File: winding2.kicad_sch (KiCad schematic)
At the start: 13 parts, among them J1 Screw_Terminal_01x06, J2 Screw_Terminal_01x04, J3 Screw_Terminal_01x04, M1 Push_Button_W12mm, SW1 RotaryEncoder_Switch, U1 TMC2209_SILENTSTEPSTICK

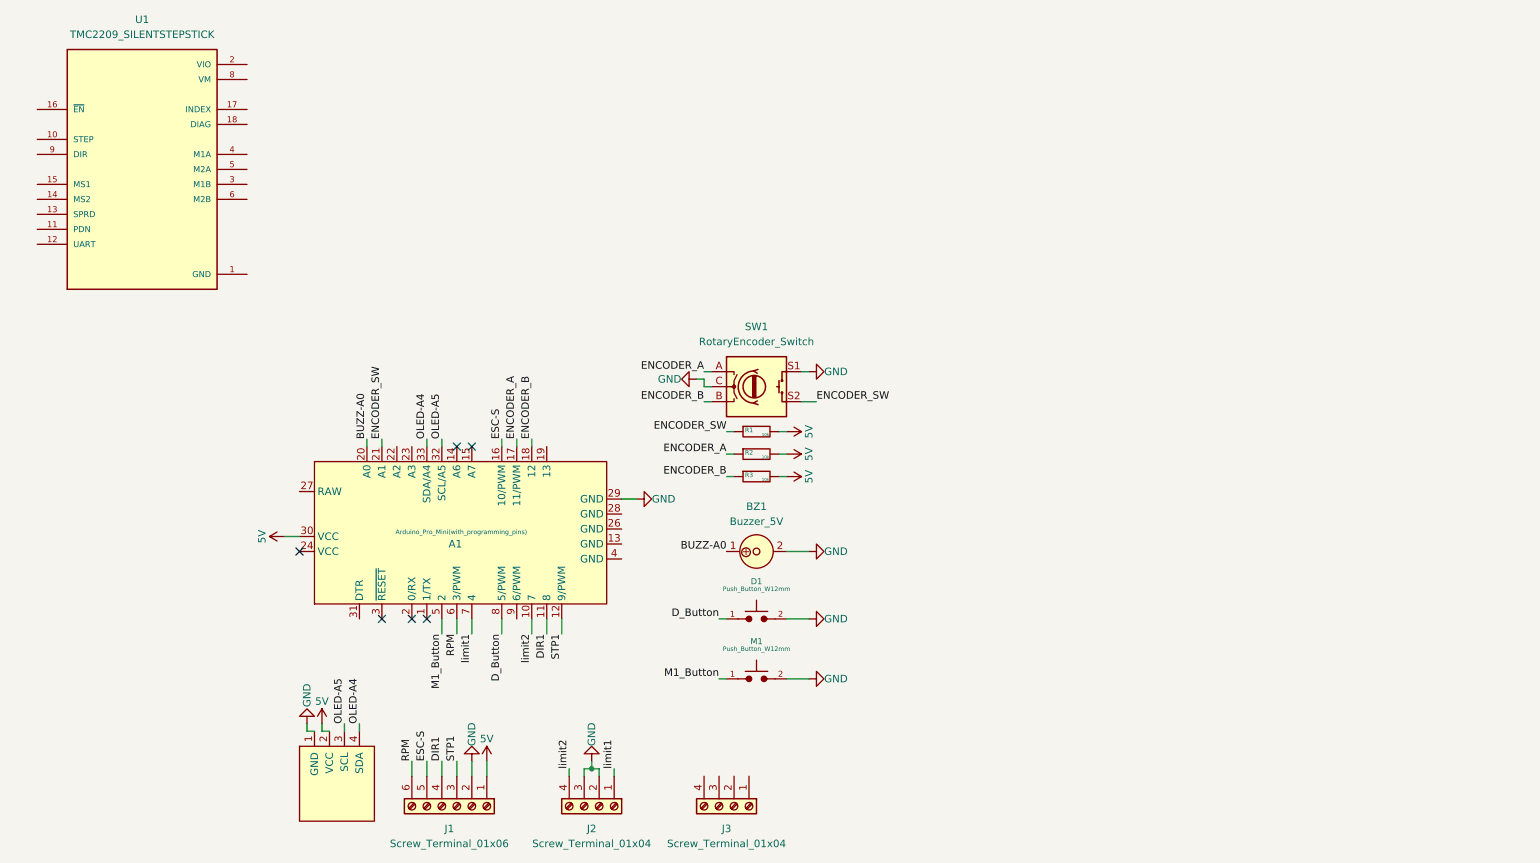
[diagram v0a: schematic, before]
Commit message: Adding the second TMC2209 stepper driver and wiring both drivers
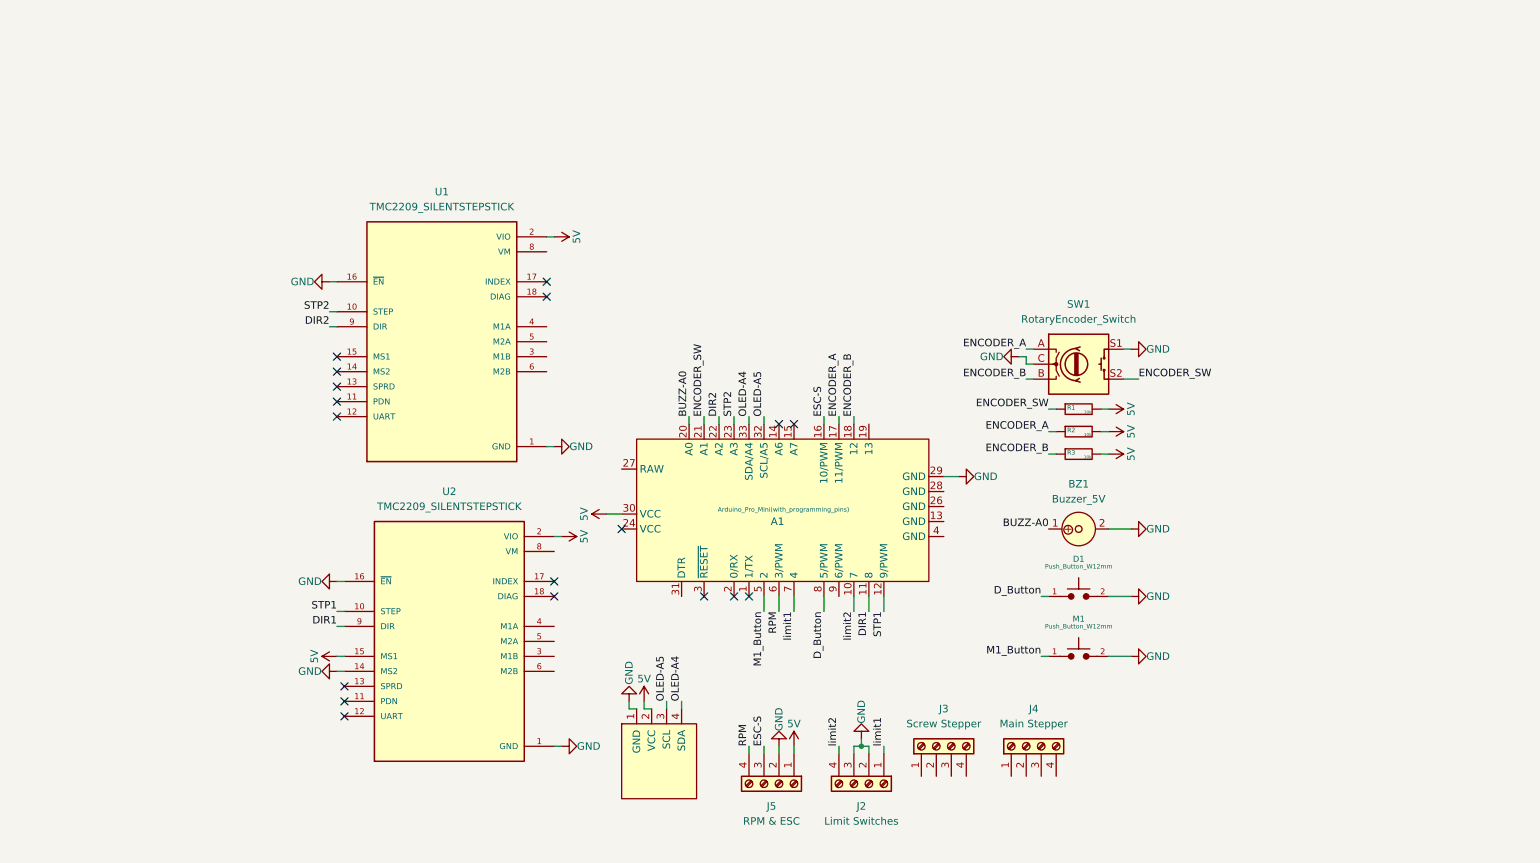
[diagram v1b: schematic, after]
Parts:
- removed J1: Screw_Terminal_01x06, Connector_Phoenix_MSTB:PhoenixContact_MSTBA_2,5_6-G-5,08_1x06_P5.08mm_Horizontal, symbol Connector:Screw_Terminal_01x06
- added J4: Main Stepper, Connector_Phoenix_MSTB:PhoenixContact_MSTBA_2,5_4-G-5,08_1x04_P5.08mm_Horizontal, symbol Connector:Screw_Terminal_01x04
- added J5: RPM & ESC, Connector_Phoenix_MSTB:PhoenixContact_MSTBA_2,5_4-G-5,08_1x04_P5.08mm_Horizontal, symbol Connector:Screw_Terminal_01x04
- added U2: TMC2209_SILENTSTEPSTICK, TMC2209_SILENTSTEPSTICK:MODULE_TMC2209_SILENTSTEPSTICK, symbol TMC2209_SILENTSTEPSTICK:TMC2209_SILENTSTEPSTICK
- J2: value Screw_Terminal_01x04 -> Limit Switches
- J3: value Screw_Terminal_01x04 -> Screw Stepper
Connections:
- net 5V: now also U1.2 (VIO), J5.1 (Pin_1), U2.15 (MS1), U2.2 (VIO)
- net DIR1: now also U2.9 (DIR)
- net ESC-S: now also J5.3 (Pin_3)
- net GND: now also U1.16 (~{EN}), J5.2 (Pin_2), U2.1 (GND), U2.14 (MS2), U2.16 (~{EN}), U2.7 (GND)
- net RPM: now also J5.4 (Pin_4)
- net STP1: now also U2.10 (STEP)
- net DIR2: now reaches A1.22 (A2)
- net DIR2: now also U1.9 (DIR)
- net STP2: now reaches A1.23 (A3)
- net STP2: now also U1.10 (STEP)
- no-connect marks 6 -> 18
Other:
- moved on the sheet: A1, BZ1, D1, J2, J3, M1, R1, R2, R3, SW1, U1

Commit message: finalize the schematic part and footprints assigning step
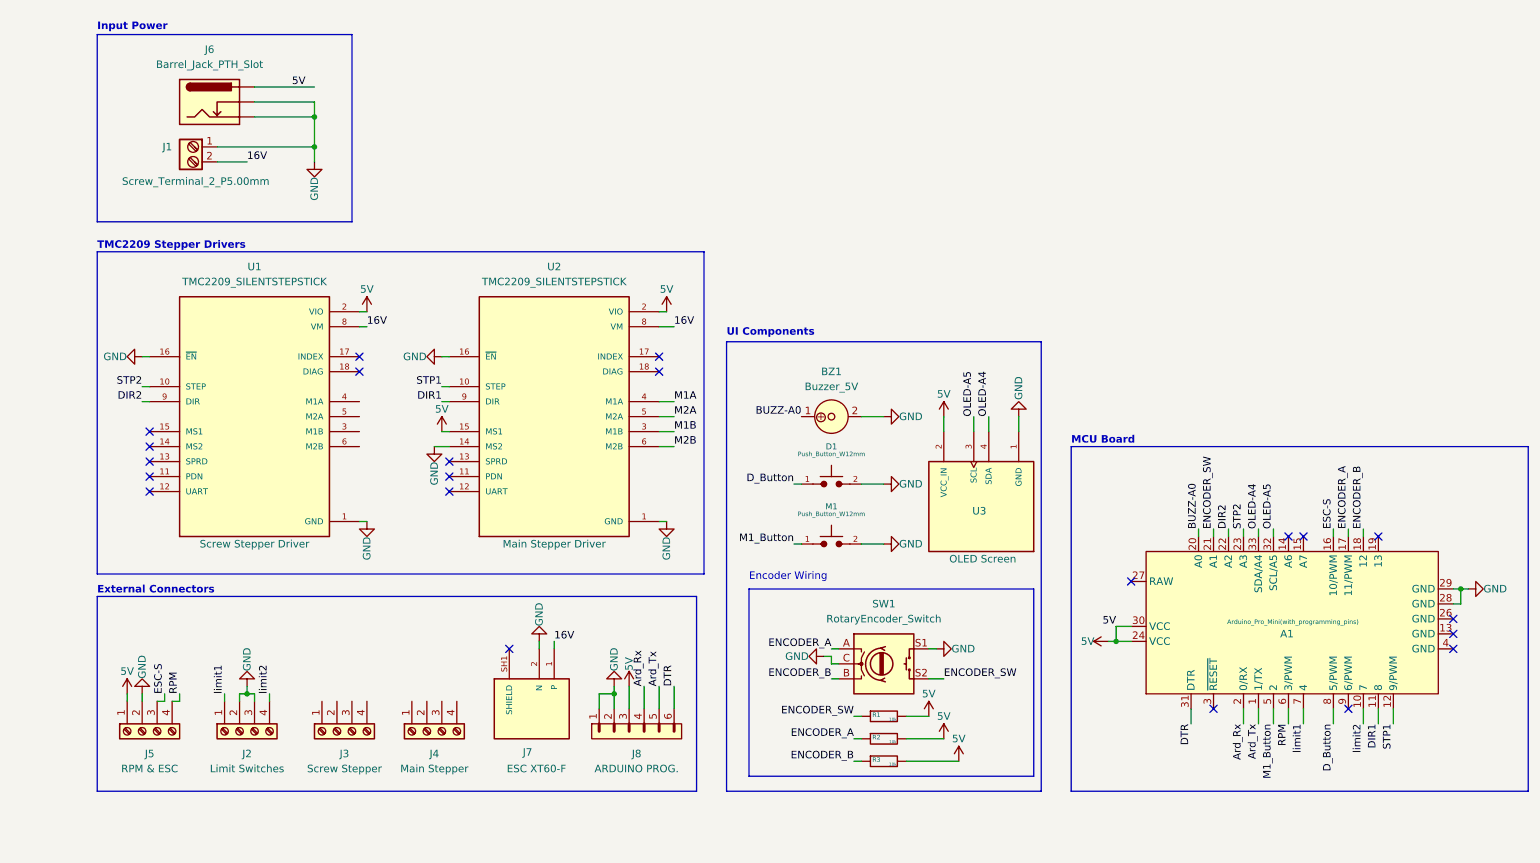
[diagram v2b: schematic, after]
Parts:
- removed Brd1: SSD1306, SSD1306:128x64OLED, symbol SSD1306-128x64_OLED:SSD1306
- added J1: Screw_Terminal_2_P5.00mm, Connector_Phoenix_MSTB:PhoenixContact_MSTBA_2,5_2-G-5,08_1x02_P5.08mm_Horizontal, symbol PCM_SL_Screw_Terminal:Screw_Terminal_2_P5.00mm
- added J6: Barrel_Jack_PTH_Slot, PCM_SparkFun-Connector:Barrel_Jack_PTH_Slot, symbol PCM_SparkFun-Connector:Barrel_Jack_PTH_Slot
- added J7: ESC XT60-F, XT60PW-F:AMASS_XT60PW-F, symbol XT60PW-F:XT60PW-F
- added J8: ARDUINO PROG., Connector_PinHeader_2.54mm:PinHeader_1x06_P2.54mm_Vertical, symbol PCM_SL_Pin_Headers:PINHD_1x6_Male
- added U3: DM-OLED096-636, DM-OLED096-636:MODULE_DM-OLED096-636, symbol DM-OLED096-636:DM-OLED096-636
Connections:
- net 5V: now also A1.24 (VCC), J6.PWR, J8.3, U3.2 (VCC_IN)
- net GND: now also A1.28 (GND), J1.1, J6.GND, J6.GNDBREAK, J7.2 (N), J8.1, J8.2, U3.1 (GND)
- net OLED-A4: now also U3.4 (SDA)
- net OLED-A5: now also U3.3 (SCL)
- net M1B: now reaches U2.3 (M1B)
- net M1A: now reaches U2.4 (M1A)
- net M2A: now reaches U2.5 (M2A)
- net M2B: now reaches U2.6 (M2B)
- net 16V: now reaches U2.8 (VM)
- net 16V: now also U1.8 (VM), J1.2, J7.1 (P)
- net Ard_Tx: now reaches A1.1 (1/TX)
- net Ard_Tx: now also J8.5
- net Ard_Rx: now reaches A1.2 (0/RX)
- net Ard_Rx: now also J8.4
- net DTR: now reaches A1.31 (DTR)
- net DTR: now also J8.6
- new net: J7.SH1 (SHIELD), J7.SH2 (SHIELD)
- no-connect marks 18 -> 22
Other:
- note added: "Encoder Wiring"
- note added: "External Connectors"
- note added: "Input Power"
- note added: "MCU Board"
- note added: "TMC2209 Stepper Drivers"
- note added: "UI Components"
- moved on the sheet: A1, BZ1, D1, J2, J3, J4, J5, M1, R1, R2, R3, SW1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

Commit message: fix: adding missing stepper motors connections and PWR_FLAG labels
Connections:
- net M1A: now also J4.2 (Pin_2)
- net M1B: now also J4.1 (Pin_1)
- net M2A: now also J4.3 (Pin_3)
- net M2B: now also J4.4 (Pin_4)
- net S1B: now reaches J3.1 (Pin_1)
- net S1B: now also U1.3 (M1B)
- net S1A: now reaches J3.2 (Pin_2)
- net S1A: now also U1.4 (M1A)
- net S2A: now reaches J3.3 (Pin_3)
- net S2A: now also U1.5 (M2A)
- net S2B: now reaches J3.4 (Pin_4)
- net S2B: now also U1.6 (M2B)

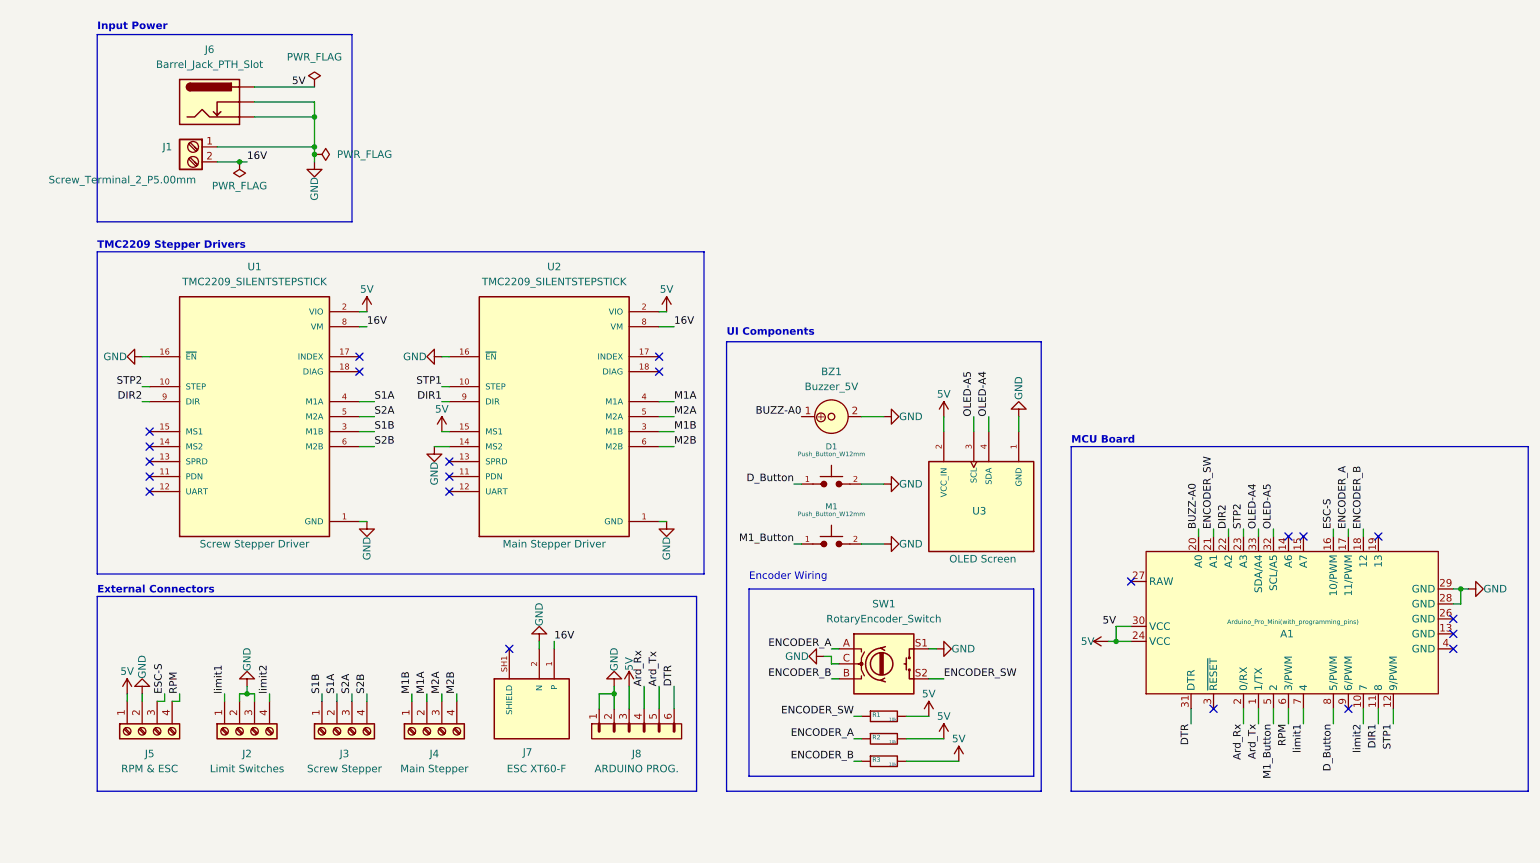
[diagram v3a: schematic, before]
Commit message: Manual routing with ground plan - v0.0
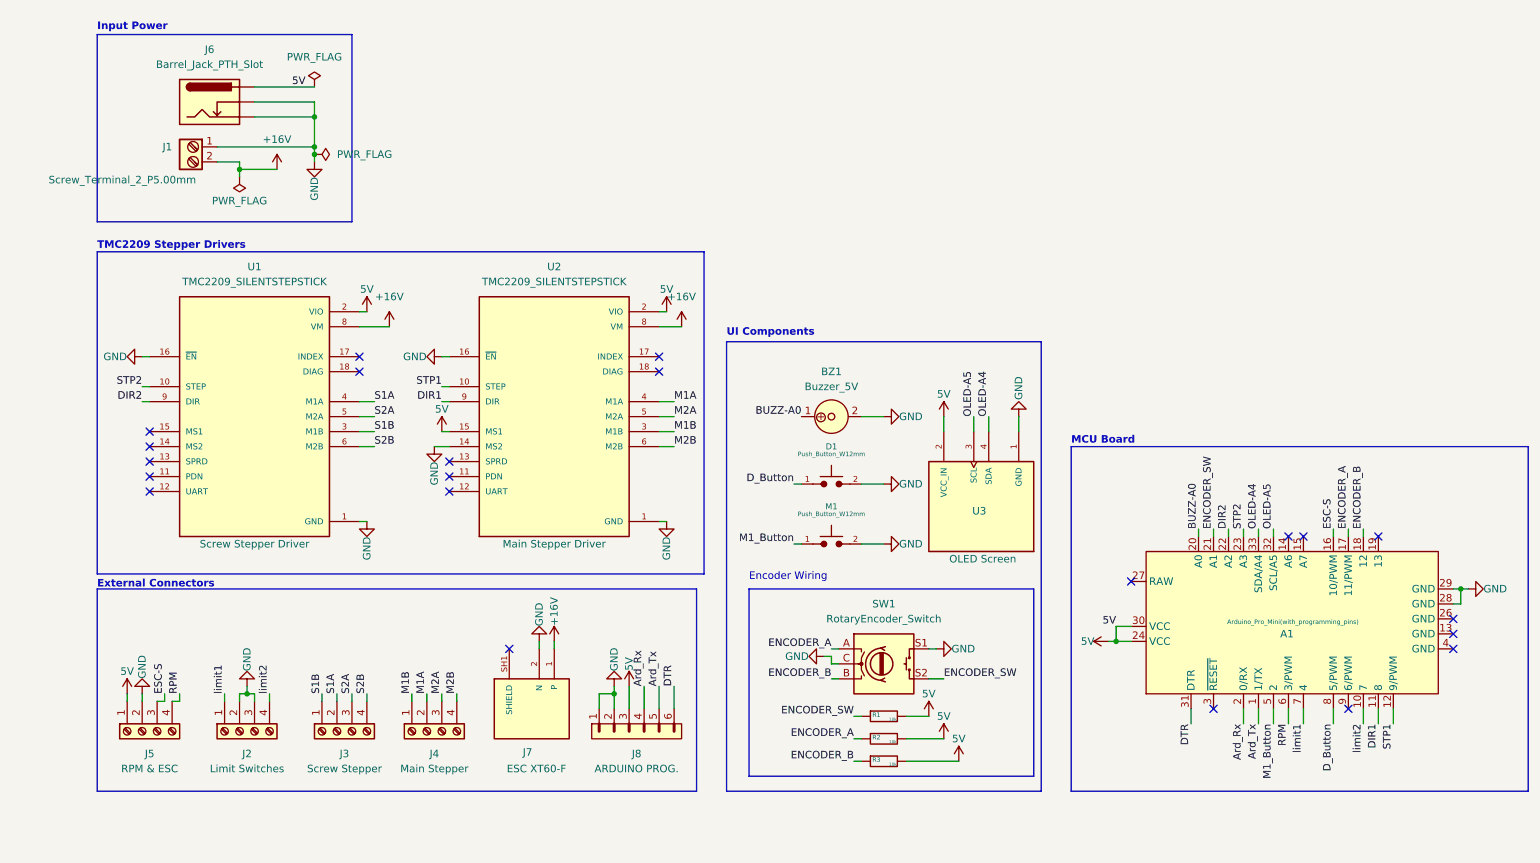
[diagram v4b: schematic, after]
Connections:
- net 16V renamed +16V

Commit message: version added to sch and pcb sheets
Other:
- title: (none) -> PCB
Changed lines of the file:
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@@
 	(generator_version "9.0")
 	(paper "A4")
+	(title_block
+		(title "PCB")
+		(rev "0.0")
+	)
 	(rectangle
 		(start 31.75 60.96)
